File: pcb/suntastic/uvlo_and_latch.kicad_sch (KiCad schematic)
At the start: 38 parts, among them U1 TLV3691IDCKR, U2 REF35102QDBVR, U3 REF35409QDBVR, U4 TLV3691IDCKR, U5 TC7WH02FU_LJCT

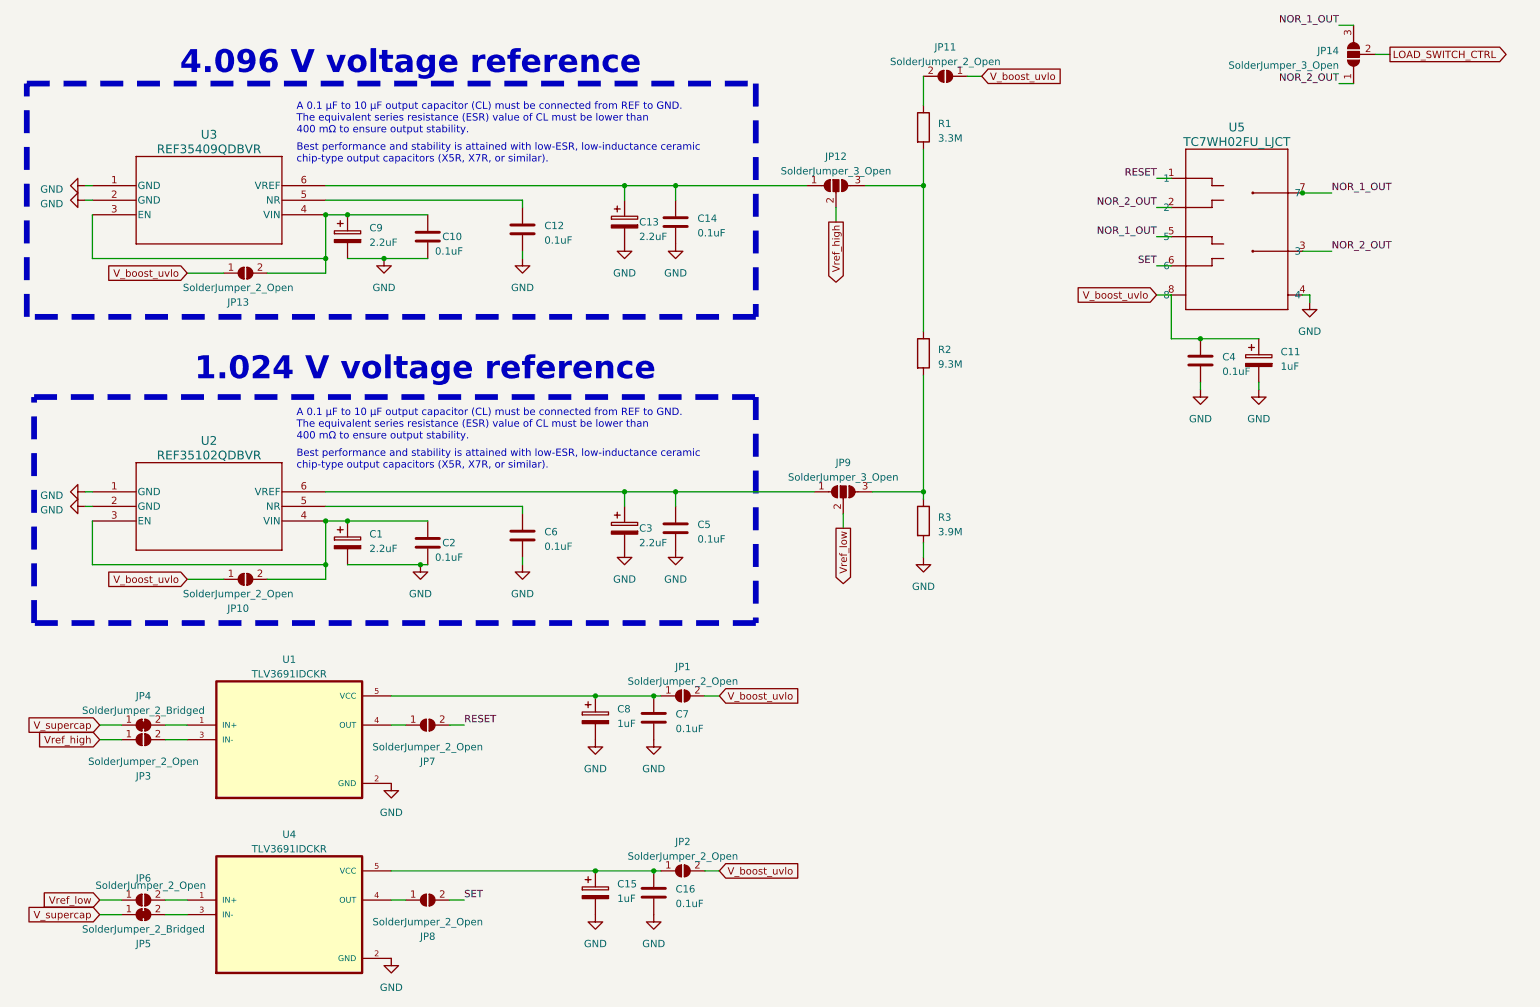
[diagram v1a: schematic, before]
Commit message: Add load switch and RAK connector
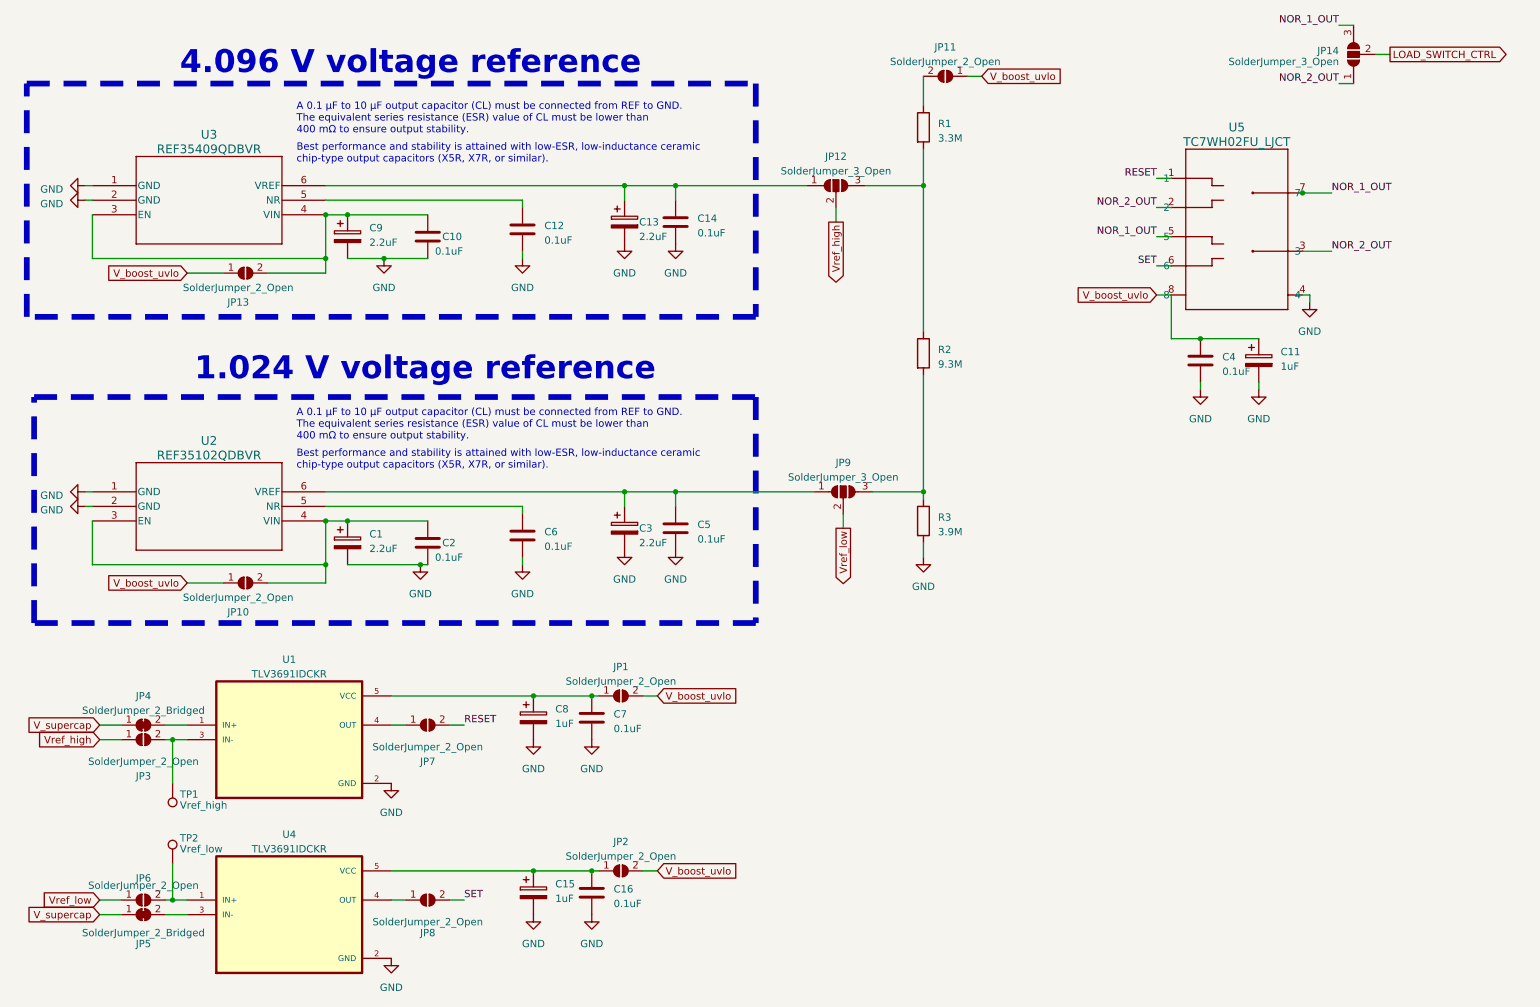
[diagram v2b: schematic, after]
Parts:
- added TP1: Vref_high, symbol Connector:TestPoint
- added TP2: Vref_low, symbol Connector:TestPoint
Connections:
- net at JP6.2 (B), U4.1 (IN+): now also TP2.1
- net at JP3.2 (B), U1.3 (IN-): now also TP1.1
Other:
- moved on the sheet: C15, C16, C7, C8, JP1, JP10, JP2

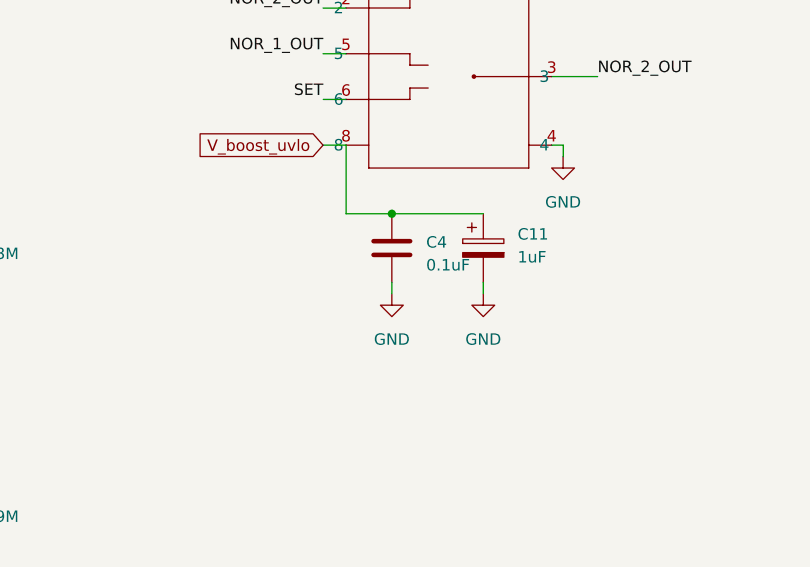
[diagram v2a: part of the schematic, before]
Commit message: Update footprints
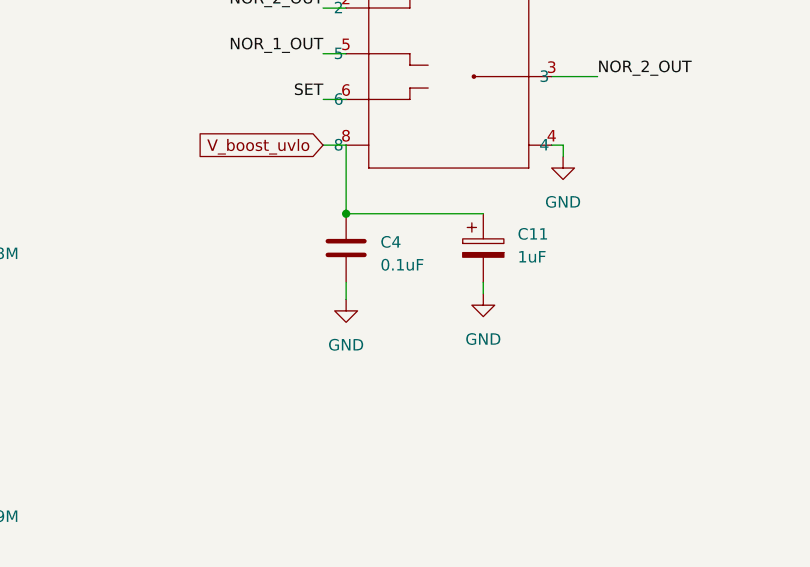
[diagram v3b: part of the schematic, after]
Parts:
- C10, C12, C14, C16, C4, C7: footprint (none) -> Capacitor_SMD:C_0603_1608Metric_Pad1.08x0.95mm_HandSolder
- R1, R2, R3: footprint (none) -> Resistor_SMD:R_0603_1608Metric_Pad0.98x0.95mm_HandSolder
- TP1, TP2: footprint (none) -> TestPoint:TestPoint_Pad_D1.5mm
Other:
- moved on the sheet: C4

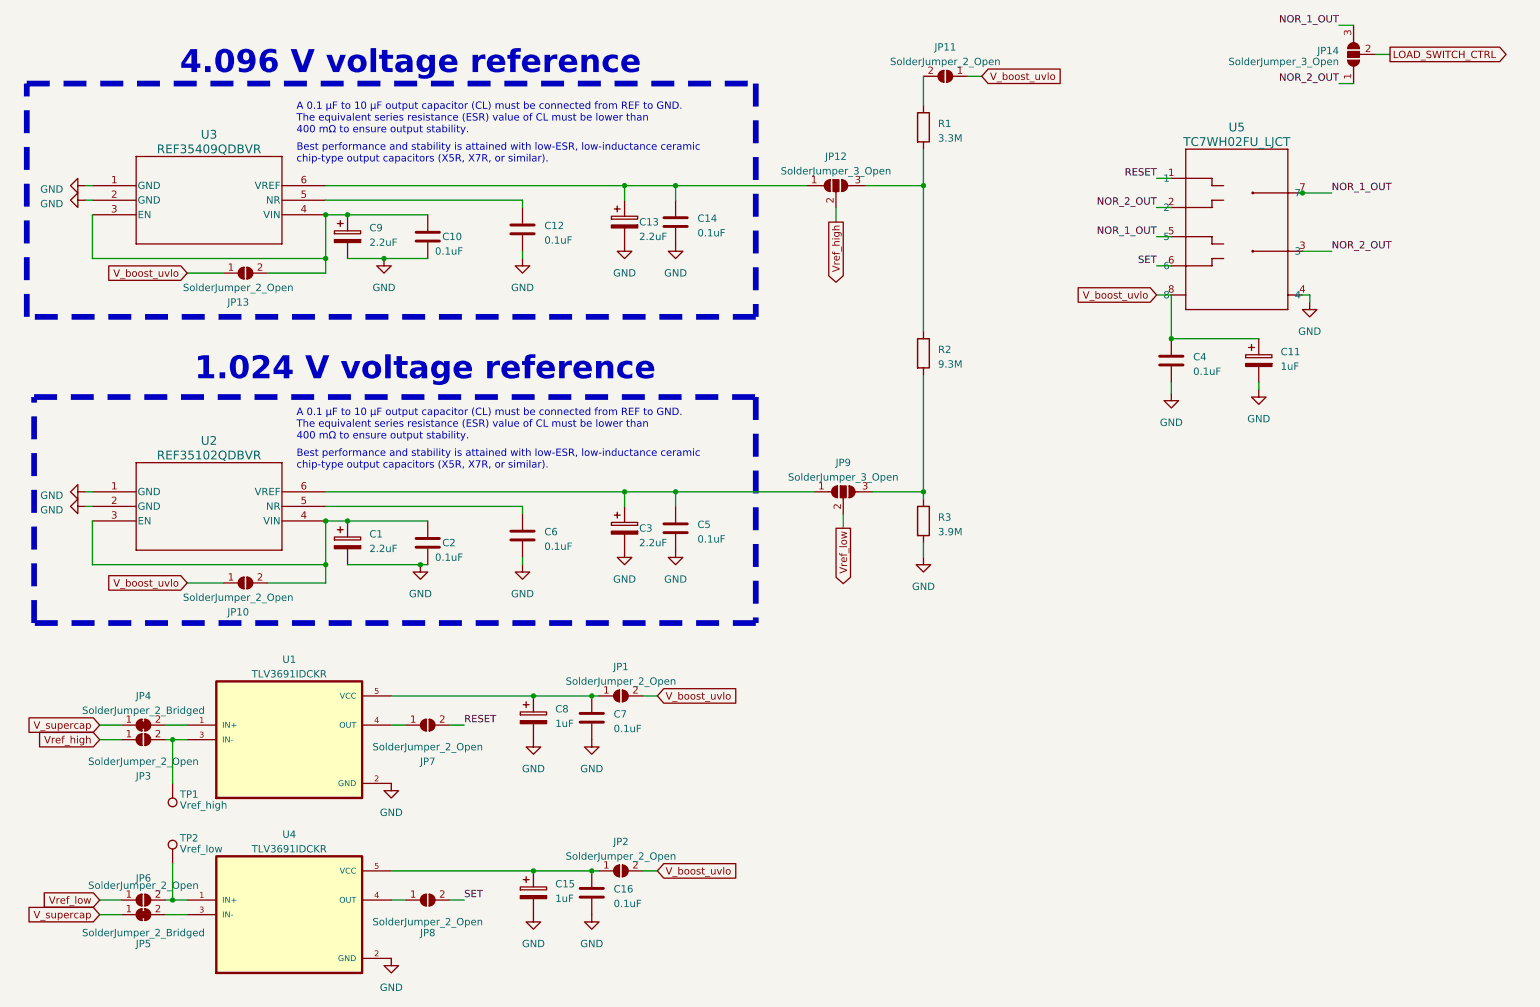
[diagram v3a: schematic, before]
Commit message: Update more footprints and start with PCB
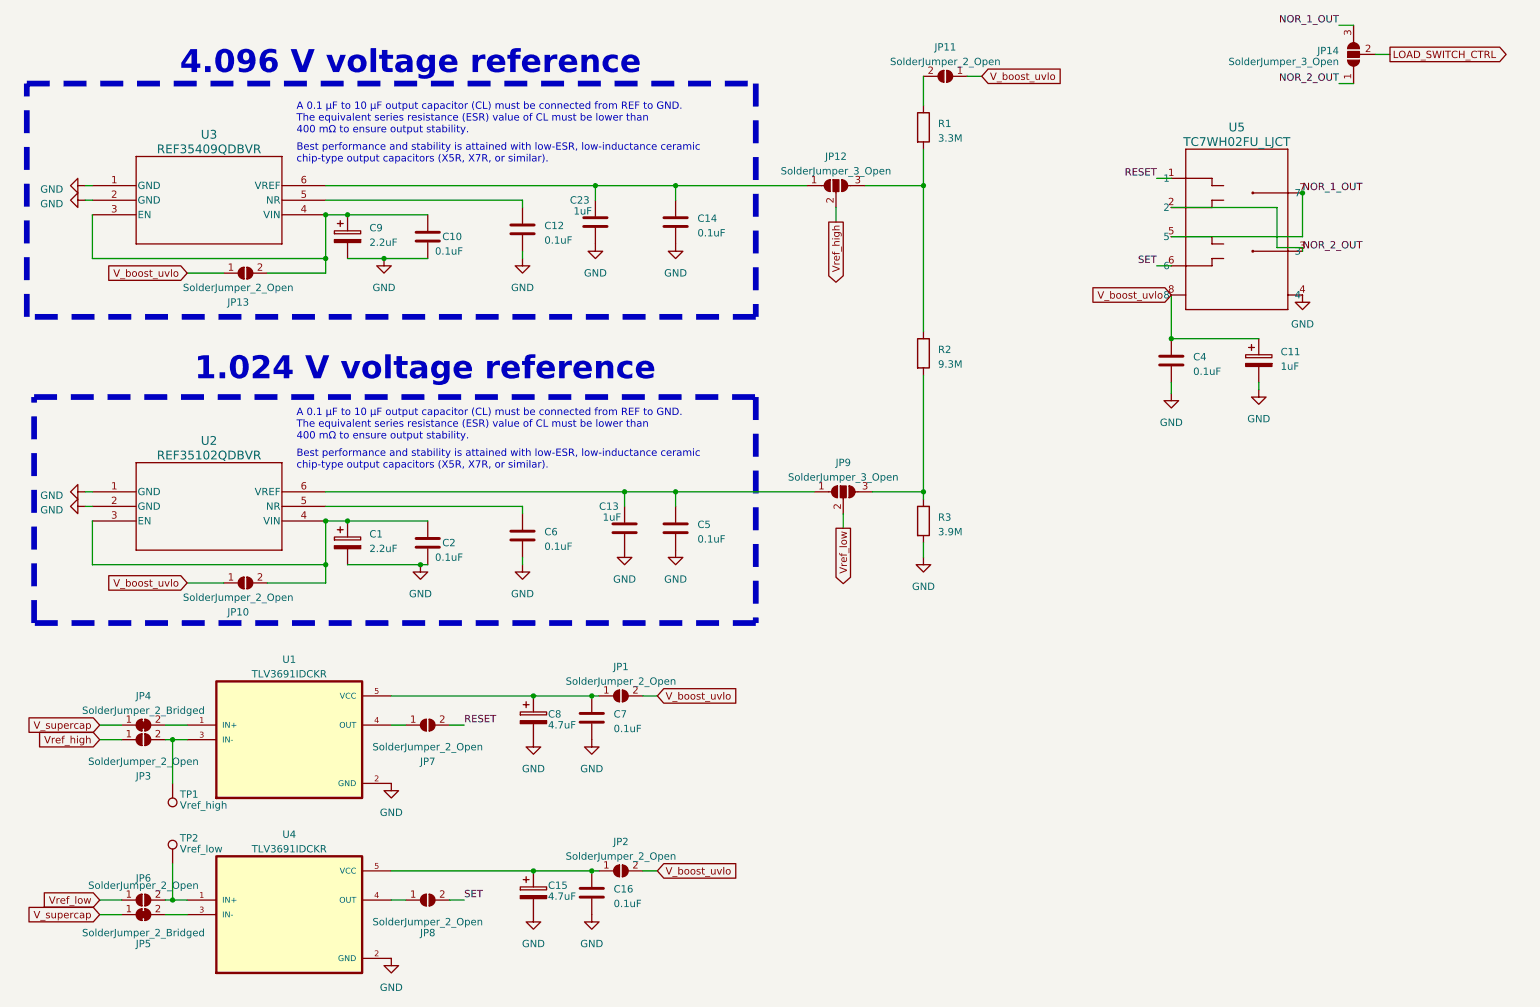
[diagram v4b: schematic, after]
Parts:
- removed C13, C3: 2.2uF, symbol Device:C_Polarized
- added C13, C23: 1uF, Capacitor_SMD:C_0603_1608Metric_Pad1.08x0.95mm_HandSolder, symbol Device:C
- C1, C9: footprint (none) -> Capacitor_SMD:CP_Elec_4x5.4
- C11: footprint (none) -> Capacitor_SMD:CP_Elec_4x4.5
- C15, C8: value 1uF -> 4.7uF; footprint (none) -> Capacitor_SMD:CP_Elec_4x5.4
- C2, C5, C6: footprint (none) -> Capacitor_SMD:C_0603_1608Metric_Pad1.08x0.95mm_HandSolder
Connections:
- net GND: now also U5.4, C13.2, C23.2
- net NOR_1_OUT: now also U5.5
- net NOR_2_OUT: now also U5.2
- net V_boost_uvlo: now also C11.1, C4.1, U5.8
- net at C5.1, JP9.1 (A), U2.6 (VREF): now also C13.1
- net at C14.1, JP12.1 (A), U3.6 (VREF): now also C23.1

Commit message: Rework watchdog
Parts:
- U5: footprint Package_SO:Zetex_SM8 -> Package_SO:TSSOP-8_3x3mm_P0.65mm
